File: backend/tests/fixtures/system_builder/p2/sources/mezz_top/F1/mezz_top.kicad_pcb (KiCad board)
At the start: 2 copper layers, 50 x 40 mm, 2 parts, among them J1 DF12_Receptacle_2x10, J2 DF12_Receptacle_2x10

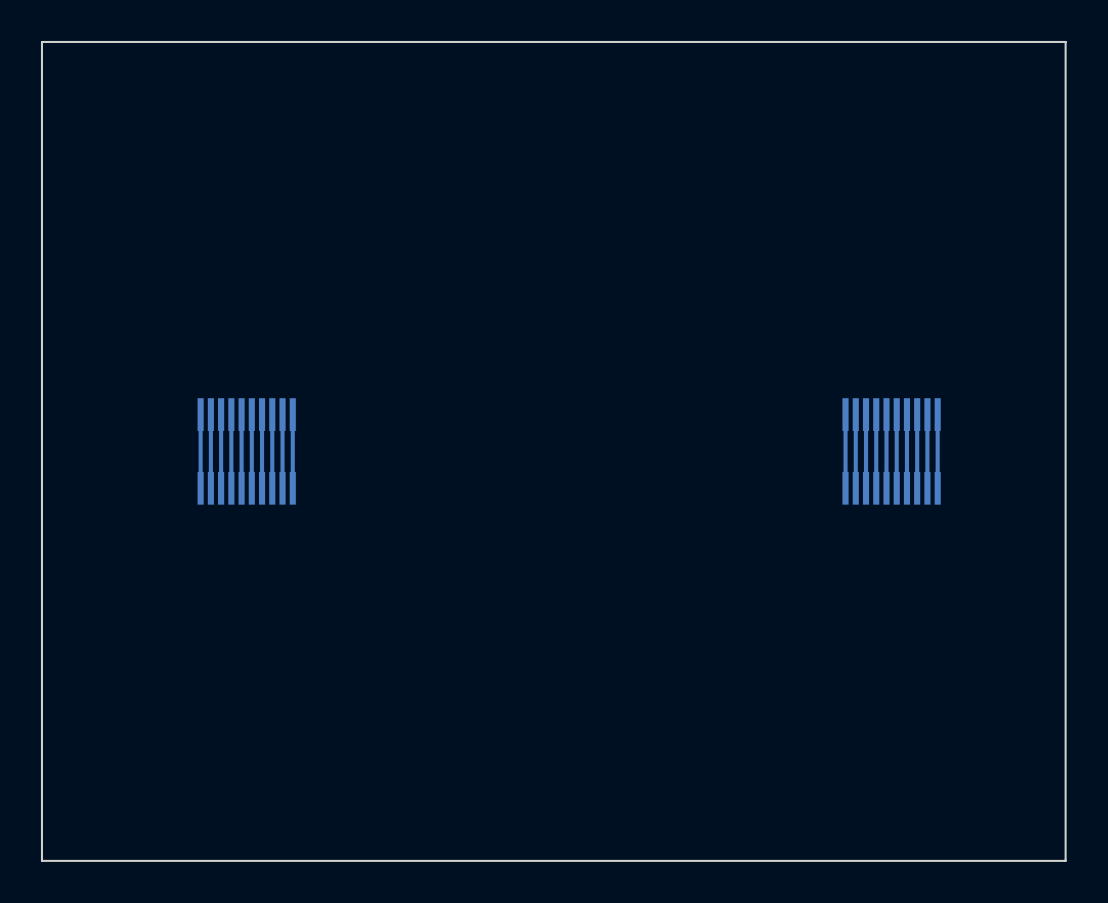
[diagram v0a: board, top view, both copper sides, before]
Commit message: SB2-21: rebuild the mezzanine fixtures on Samtec ADM6/ADF6
The SB2-21 review moved the mezzanine pair from Hirose DF12(3.0) to Samtec
ADM6-30-03.5-L-4-0-A / ADF6-30-03.5-L-4-0-A, the JTYU OBC-to-CMBD pair.

- Footprints are written from Samtec's recommended PCB layouts (ADM6 rev G,
  ADF6 rev H): 4x30 at 0.635 mm, 0.356 mm pads, -A alignment NPTHs. They
  match Pixxel's ADM6-30 library footprint and CMBD's ADF6-30 pad for pad.
- Goldens: mated height 7.00 mm (ADX6 mated views, Table 1), top pose
  (0, 0, 8.6) mm, body heights G 4.900 / K 3.230 mm. The footprints name no
  orientation, so frames infer at medium confidence; goldens now pin the
  confidence of every frame.
- Samtec's STEP files (git-ignored, from the JTYU repos) are placed with
  rotate (-90 0 0); their alignment pins land on the NPTHs in KiCad's GLB
  export, which fixes the pin-1 end.
- All six boards clean on ERC, DRC with schematic parity, netlist, STEP and
  GLB with KiCad 10.0.6.
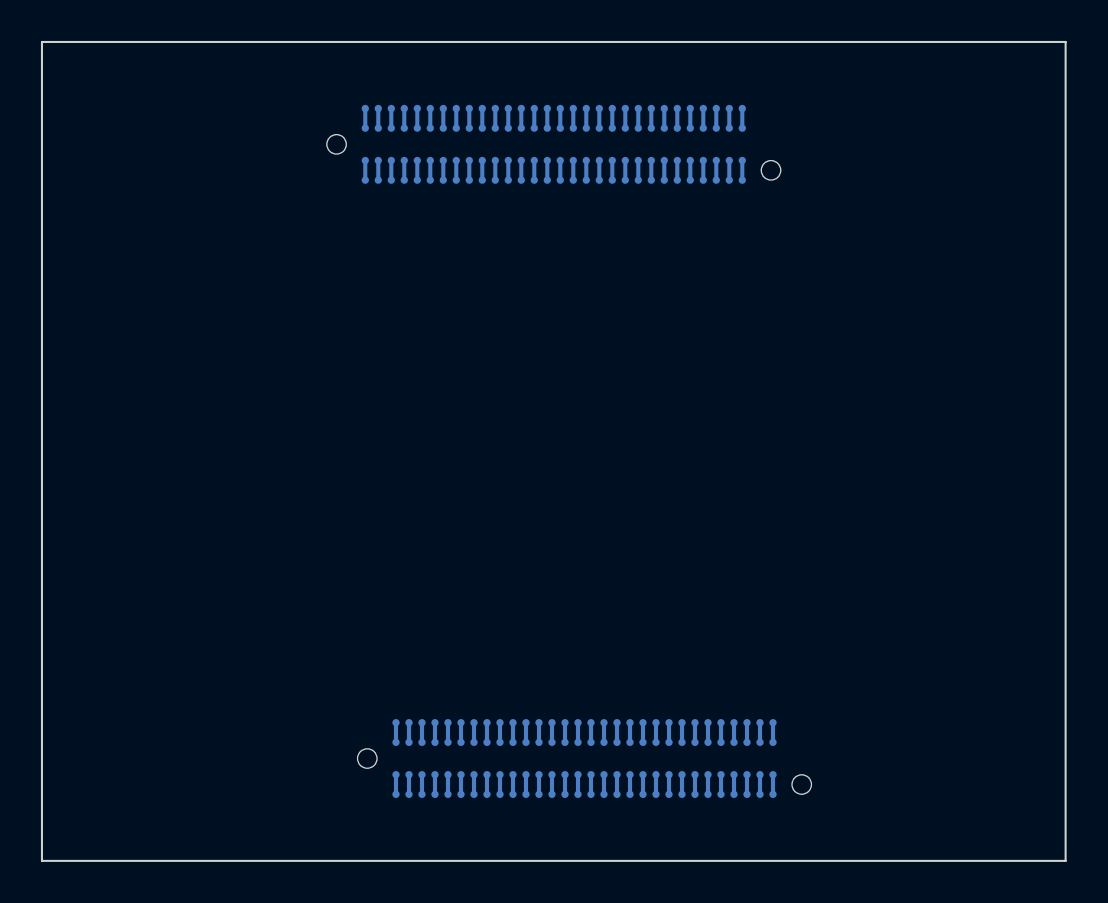
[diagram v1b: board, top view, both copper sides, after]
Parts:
- J1, J2: value DF12_Receptacle_2x10 -> ADF6_4x30; footprint PrismFixture:Hirose_DF12_DF12C3.0-20DS-0.5V_2x10_P0.50mm_Vertical -> PrismFixture:Samtec_ADF6-30-03.5-L-4-0-A
- moved J1 21.2 mm to (125.0, 105.0)
- moved J2 21.2 mm to (126.5, 135.0)
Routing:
- net /B9: track 3.60 -> 0.00 mm
- net /B8: track 3.60 -> 0.00 mm
- net /B7: track 3.60 -> 0.00 mm
- net /B6: track 3.60 -> 0.00 mm
- net /B5: track 3.60 -> 0.00 mm
- net /B4: track 3.60 -> 0.00 mm
- net /B3: track 3.60 -> 0.00 mm
- net /B2: track 3.60 -> 0.00 mm
- net /B10: track 3.60 -> 0.00 mm
- net /B1: track 3.60 -> 0.00 mm
- net /A9: track 3.60 -> 0.00 mm
- net /A8: track 3.60 -> 0.00 mm
- net /A7: track 3.60 -> 0.00 mm
- net /A6: track 3.60 -> 0.00 mm
- net /A5: track 3.60 -> 0.00 mm
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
